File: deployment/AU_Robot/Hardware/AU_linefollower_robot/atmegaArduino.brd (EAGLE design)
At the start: 53 x 82.5 mm, 11 parts

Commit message: updated arduino sw
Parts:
- added LED1, LED2, LED3: (no value), eagle-ltspice:LED_LD260
- added R1, R2, R3: 270, rcl:0204/5
- C1: device rcl:E1,8-4 -> rcl:C050-025X075
- JTAG: value (none) -> 2510-; device con-ml:ML10L -> con-3m:PAK100/2500-10
- moved JTAG 6.48 mm to (8.89, 68.6), flipped to the top, turned to 0 degrees
- moved C1 1.80 mm to (12.7, 49.5), turned to 0 degrees
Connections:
- new net N$11: LED1.K, R3.2
- new net N$14: LED2.K, R2.2
- new net N$16: LED3.K, R1.2
- new net N$17: IC1.20, LED1.A
- new net N$18: IC1.19, LED2.A
- new net N$19: IC1.18, LED3.A
- new net N$20: IC1.16, IOH.2
- new net N$21: IC1.17, IOH.1
- net GND: now also C1.2, R1.1, R2.1, R3.1; no longer C1.-
- net N$1: now also IC1.14; no longer IC1.15
- net N$2: now also IC1.15; no longer IC1.14
- net VCC: now also C1.1, IC1.10; no longer C1.+
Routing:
- net VCC: track 116.0 -> 204.5 mm, vias 6 -> 10
- net N$21: track 0.00 -> 61.0 mm, vias 0 -> 2
- net N$20: track 0.00 -> 55.9 mm, vias 0 -> 2
- net N$3: track 8.89 -> 52.1 mm, vias 0 -> 2
- net N$15: track 100.3 -> 62.2 mm, vias 6 -> 2
- net GND: track 248.0 -> 278.5 mm, vias 1 -> 3
- net N$6: track 11.4 -> 16.5 mm, vias 0 -> 2
- net N$18: track 0.00 -> 3.81 mm
- net N$17: track 0.00 -> 3.81 mm
- net N$2: track 45.7 -> 48.3 mm
- net N$16: track 0.00 -> 2.54 mm
- net N$14: track 0.00 -> 2.54 mm
- net N$11: track 0.00 -> 2.54 mm
- net N$1: track 50.8 -> 48.3 mm, vias 2 -> 0
- net N$4: track 14.0 -> 11.4 mm, vias 2 -> 1
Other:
- board size 53 x 82.5 mm -> 53 x 83.8 mm

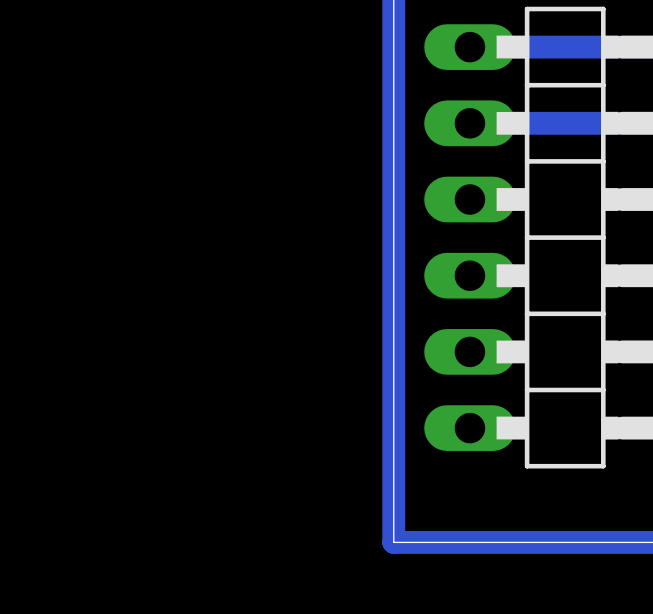
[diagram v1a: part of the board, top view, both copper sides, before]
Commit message: updated schematics
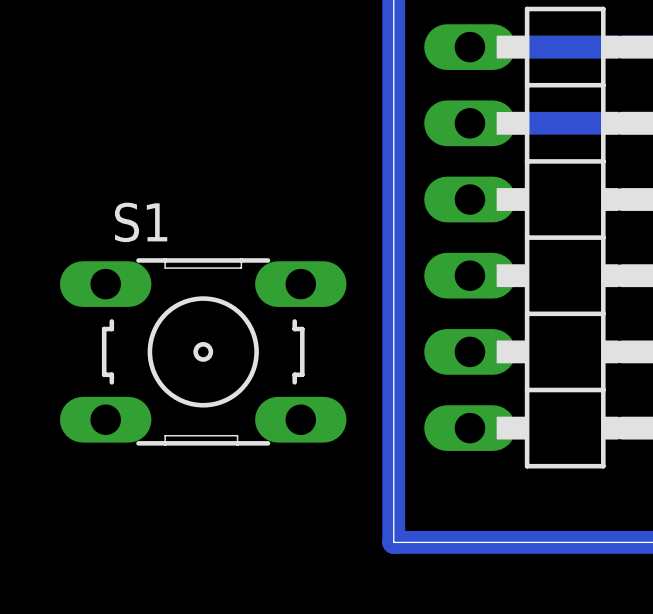
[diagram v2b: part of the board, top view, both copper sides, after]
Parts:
- added S1: (no value), switch-omron:B3F-10XX
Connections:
- new net N$22: IOL.3
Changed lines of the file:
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@@
 <element name="R2" library="rcl" package="0204/5" value="270" x="44.45" y="72.39" rot="R180"/>
 <element name="R3" library="rcl" package="0204/5" value="270" x="44.45" y="74.93" rot="R180"/>
+<element name="S1" library="switch-omron" package="B3F-10XX" value="" x="-7.62" y="3.81">
+<attribute name="MPN" value="B3F-1000" x="-7.62" y="3.81" size="1.778" layer="27" display="off"/>
+<attribute name="OC_FARNELL" value="176432" x="-7.62" y="3.81" size="1.778" layer="27" display="off"/>
+<attribute name="OC_NEWARK" value="36M3542" x="-7.62" y="3.81" size="1.778" layer="27" display="off"/>
+<attribute name="MF" value="" x="-7.62" y="3.81" size="1.778" layer="27" display="off"/>
+</element>
 </elements>
 <signals>
@@
 <wire x1="40.64" y1="67.31" x2="33.02" y2="67.31" width="0.254" layer="16"/>
 </signal>
+<signal name="N$22">
+<contactref element="IOL" pad="3"/>
+</signal>
 </signals>
